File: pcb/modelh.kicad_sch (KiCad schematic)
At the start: 15 parts, among them J1 Battery Conn, J2 Conn_01x16, J3 Conn_01x12, J4 Conn_01x04, U1 nice_nano, U2 74HC595, U3 74HC595

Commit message: version 0.2
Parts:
- added D1, D10, D11, D12, D13, D14, D15, D16, D2, D3, D4, D5, D6, D7, D8, D9: D_Small, Library:DO-35 smaller, symbol Device:D_Small
- added J5: Conn_01x06, Connector_PinHeader_2.54mm:PinHeader_1x06_P2.54mm_Vertical, symbol Connector_Generic:Conn_01x06
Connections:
- net +3.3V: now also J5.2 (Pin_2); no longer JP5.2 (B)
- net CS: now also U1.8 (022); no longer U1.3 (008/RX)
- net GND: now also JP5.2 (B), J5.1 (Pin_1)
- net SCLK: now also U1.7 (020); no longer U1.2 (006/TX)
- net col0: now also D1.2 (A); no longer J2.1 (Pin_1)
- net col1: now also D2.2 (A); no longer J2.2 (Pin_2)
- net col10: now also D11.2 (A); no longer J2.11 (Pin_11)
- net col11: now also D12.2 (A); no longer J2.12 (Pin_12)
- net col12: now also D13.2 (A); no longer J2.13 (Pin_13)
- net col13: now also D14.2 (A); no longer J2.14 (Pin_14)
- net col14: now also D15.2 (A); no longer J2.15 (Pin_15)
- net col15: now also D16.2 (A); no longer J2.16 (Pin_16)
- net col2: now also D3.2 (A); no longer J2.3 (Pin_3)
- net col3: now also D4.2 (A); no longer J2.4 (Pin_4)
- net col4: now also D5.2 (A); no longer J2.5 (Pin_5)
- net col5: now also D6.2 (A); no longer J2.6 (Pin_6)
- net col6: now also D7.2 (A); no longer J2.7 (Pin_7)
- net col7: now also D8.2 (A); no longer J2.8 (Pin_8)
- net col8: now also D9.2 (A); no longer J2.9 (Pin_9)
- net col9: now also D10.2 (A); no longer J2.10 (Pin_10)
- net user4: now reaches U1.10 (100)
- net user4: now also J5.6 (Pin_6)
- net user3: now reaches U1.9 (024)
- net user3: now also J5.5 (Pin_5)
- new net: D1.1 (K), J2.1 (Pin_1)
- new net: D10.1 (K), J2.10 (Pin_10)
- new net: D11.1 (K), J2.11 (Pin_11)
- new net: D12.1 (K), J2.12 (Pin_12)
- new net: D13.1 (K), J2.13 (Pin_13)
- new net: D14.1 (K), J2.14 (Pin_14)
- new net: D15.1 (K), J2.15 (Pin_15)
- new net: D16.1 (K), J2.16 (Pin_16)
- new net: D2.1 (K), J2.2 (Pin_2)
- new net: D3.1 (K), J2.3 (Pin_3)
- new net: D4.1 (K), J2.4 (Pin_4)
- new net: D5.1 (K), J2.5 (Pin_5)
- new net: D6.1 (K), J2.6 (Pin_6)
- new net: D7.1 (K), J2.7 (Pin_7)
- new net: D8.1 (K), J2.8 (Pin_8)
- new net: D9.1 (K), J2.9 (Pin_9)
- new net user1: J5.3 (Pin_3), U1.2 (006/TX)
- new net user2: J5.4 (Pin_4), U1.3 (008/RX)
- no-connect marks 5 -> 1
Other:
- note added: "User"

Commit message: Rev 0.3
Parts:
- removed J2: Conn_01x16, Library:ModelH-triomate-cols16, symbol Connector_Generic:Conn_01x16
- added D17, D18, D19, D20: D_Small, Diode_SMD:D_SOD-123F, symbol Device:D_Small
- added J2: Conn_01x20, Library:ModelH-triomate-cols20, symbol Connector_Generic:Conn_01x20
- added U4: 74HC595, Package_DIP:DIP-16_W7.62mm_Socket_LongPads, symbol 74xx:74HC595
- D1, D10, D11, D12, D13, D14, D15, D16, D2, D3, D4, D5, D6, D7, D8, D9: footprint Library:DO-35 smaller -> Diode_SMD:D_SOD-123F
- U2, U3: footprint PCM_Package_DIP_AKL:DIP-16_W7.62mm_Socket_LongPads -> Package_DIP:DIP-16_W7.62mm_Socket_LongPads
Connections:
- net +3.3V: now also U4.10 (~{SRCLR}), U4.16 (VCC)
- net CS: now also U4.12 (RCLK)
- net GND: now also U4.13 (~{OE}), U4.8 (GND)
- net SCLK: now also U4.11 (SRCLK)
- net col0: now also U2.7 (QH); no longer U2.15 (QA)
- net col1: now also U2.6 (QG); no longer U2.1 (QB)
- net col10: now also U3.5 (QF); no longer U3.2 (QC)
- net col11: now also U3.4 (QE); no longer U3.3 (QD)
- net col12: now also U3.3 (QD); no longer U3.4 (QE)
- net col13: now also U3.2 (QC); no longer U3.5 (QF)
- net col14: now also U3.1 (QB); no longer U3.6 (QG)
- net col15: now also U3.15 (QA); no longer U3.7 (QH)
- net col2: now also U2.5 (QF); no longer U2.2 (QC)
- net col3: now also U2.4 (QE); no longer U2.3 (QD)
- net col4: now also U2.3 (QD); no longer U2.4 (QE)
- net col5: now also U2.2 (QC); no longer U2.5 (QF)
- net col6: now also U2.1 (QB); no longer U2.6 (QG)
- net col7: now also U2.15 (QA); no longer U2.7 (QH)
- net col8: now also U3.7 (QH); no longer U3.15 (QA)
- net col9: now also U3.6 (QG); no longer U3.1 (QB)
- net at D1.1 (K): now also J2.1 (Pin_1)
- net at D10.1 (K): now also J2.10 (Pin_10)
- net at D11.1 (K): now also J2.11 (Pin_11)
- net at D12.1 (K): now also J2.12 (Pin_12)
- net at D13.1 (K): now also J2.13 (Pin_13)
- net at D14.1 (K): now also J2.14 (Pin_14)
- net at D15.1 (K): now also J2.15 (Pin_15)
- net at D16.1 (K): now also J2.16 (Pin_16)
- net at D2.1 (K): now also J2.2 (Pin_2)
- net at D3.1 (K): now also J2.3 (Pin_3)
- net at D4.1 (K): now also J2.4 (Pin_4)
- net at D5.1 (K): now also J2.5 (Pin_5)
- net at D6.1 (K): now also J2.6 (Pin_6)
- net at D7.1 (K): now also J2.7 (Pin_7)
- net at D8.1 (K): now also J2.8 (Pin_8)
- net at D9.1 (K): now also J2.9 (Pin_9)
- net at U3.9 (QH'): now also U4.14 (SER)
- new net: D18.1 (K), J2.18 (Pin_18)
- new net: D19.1 (K), J2.19 (Pin_19)
- new net: D20.1 (K), J2.20 (Pin_20)
- new net: D17.1 (K), J2.17 (Pin_17)
- new net col16: D17.2 (A), U4.15 (QA)
- new net col17: D18.2 (A), U4.7 (QH)
- new net col18: D19.2 (A), U4.6 (QG)
- new net col19: D20.2 (A), U4.5 (QF)
- no-connect marks 1 -> 5
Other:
- note added: "Keyboard Matrix"
- moved on the sheet: J3, J4, J5, R7, R8, R9, U2, U3

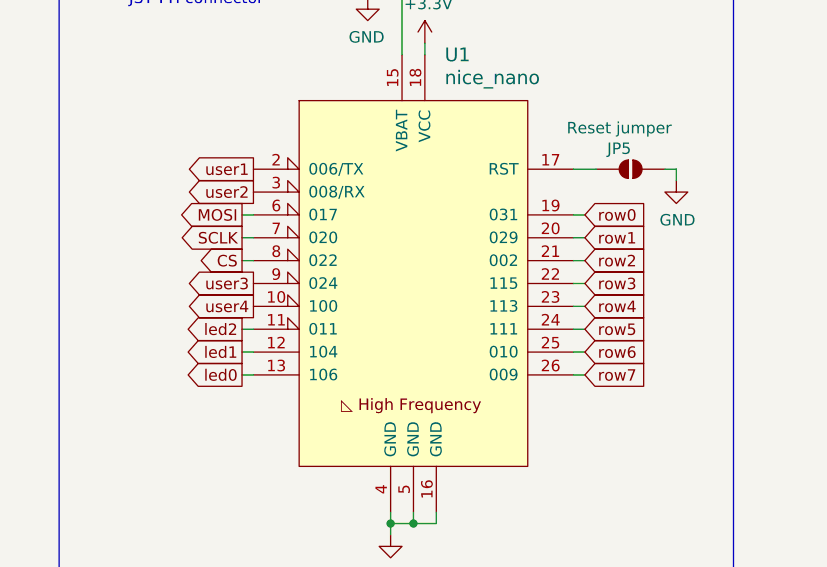
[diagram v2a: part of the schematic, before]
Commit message: Make it compatable with old pro micro
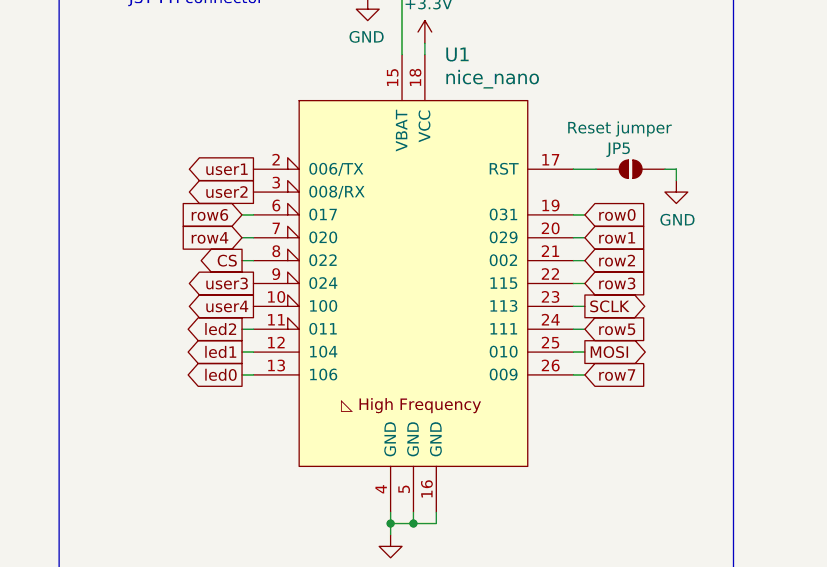
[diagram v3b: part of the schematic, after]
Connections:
- net MOSI: now also U1.25 (010); no longer U1.6 (017)
- net SCLK: now also U1.23 (113); no longer U1.7 (020)
- net row4: now also U1.7 (020); no longer U1.23 (113)
- net row6: now also U1.6 (017); no longer U1.25 (010)

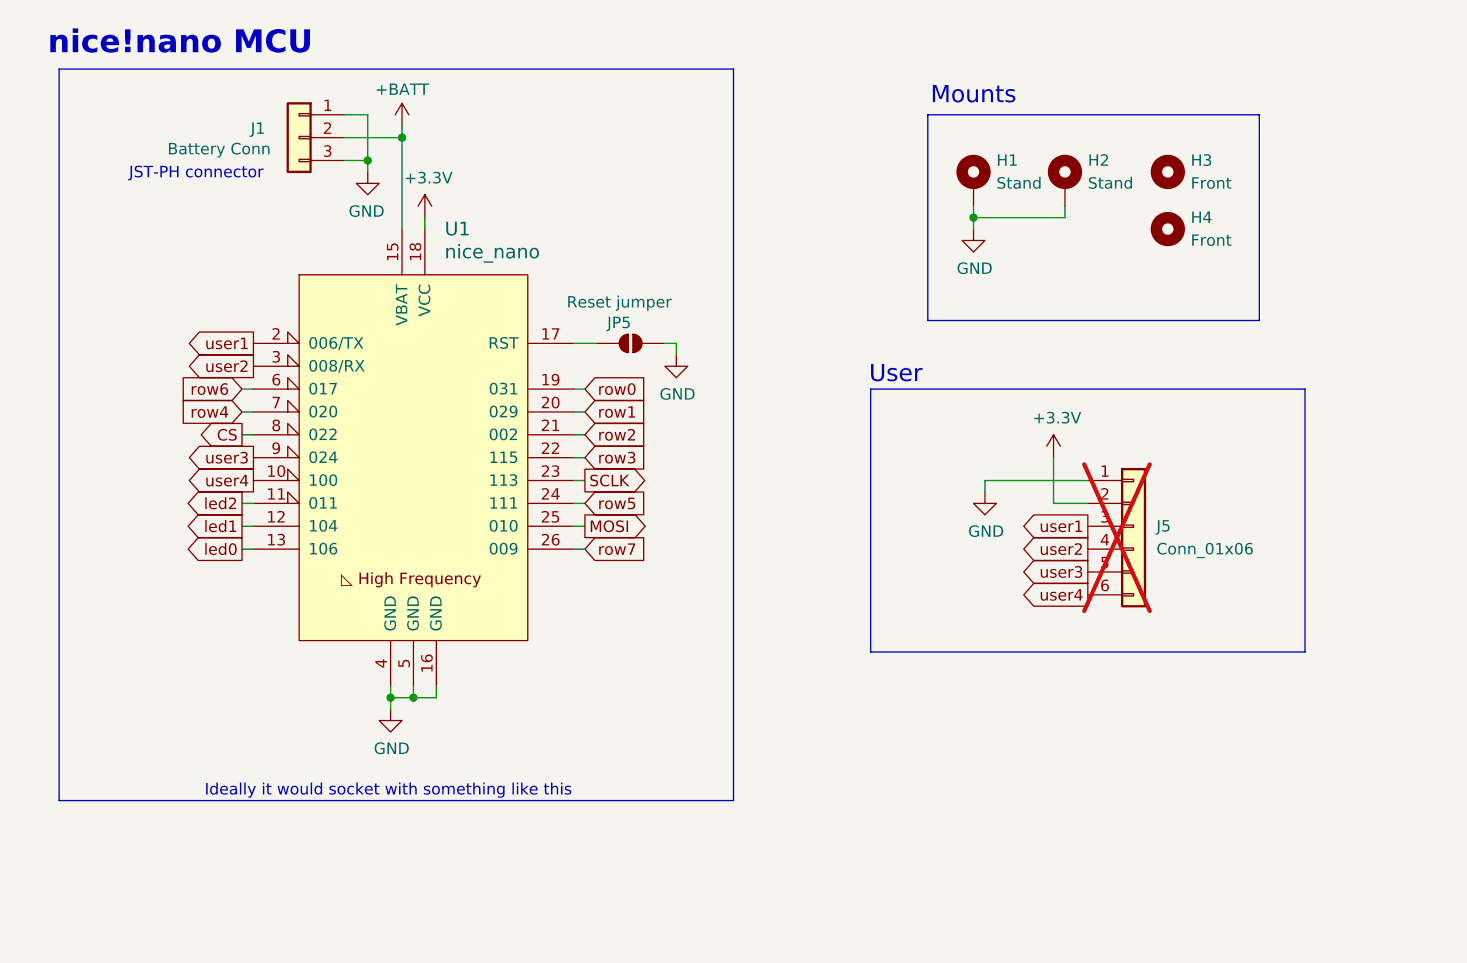
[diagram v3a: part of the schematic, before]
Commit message: v3.1; made it uncompatible because HF pins
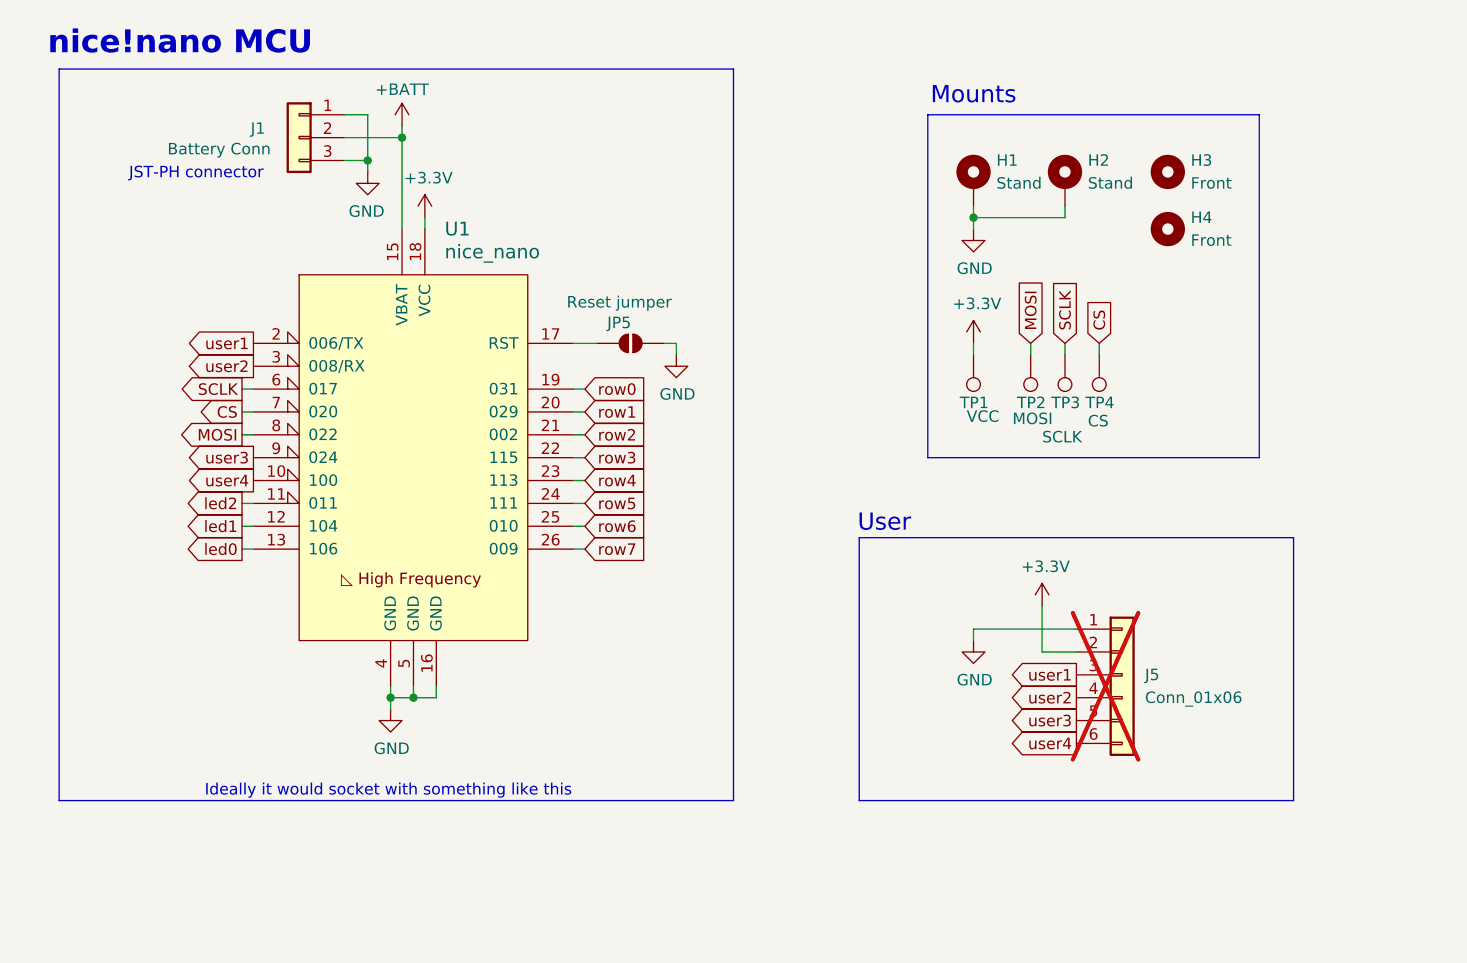
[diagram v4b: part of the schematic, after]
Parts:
- added TP1: VCC, TestPoint:TestPoint_Pad_D1.5mm, symbol Connector:TestPoint
- added TP2: MOSI, TestPoint:TestPoint_Pad_D1.0mm, symbol Connector:TestPoint
- added TP3: SCLK, TestPoint:TestPoint_Pad_D1.0mm, symbol Connector:TestPoint
- added TP4: CS, TestPoint:TestPoint_Pad_D1.0mm, symbol Connector:TestPoint
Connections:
- net +3.3V: now also TP1.1
- net CS: now also U1.7 (020), TP4.1; no longer U1.8 (022)
- net MOSI: now also U1.8 (022), TP2.1; no longer U1.25 (010)
- net SCLK: now also U1.6 (017), TP3.1; no longer U1.23 (113)
- net row4: now also U1.23 (113); no longer U1.7 (020)
- net row6: now also U1.25 (010); no longer U1.6 (017)
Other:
- moved on the sheet: J5

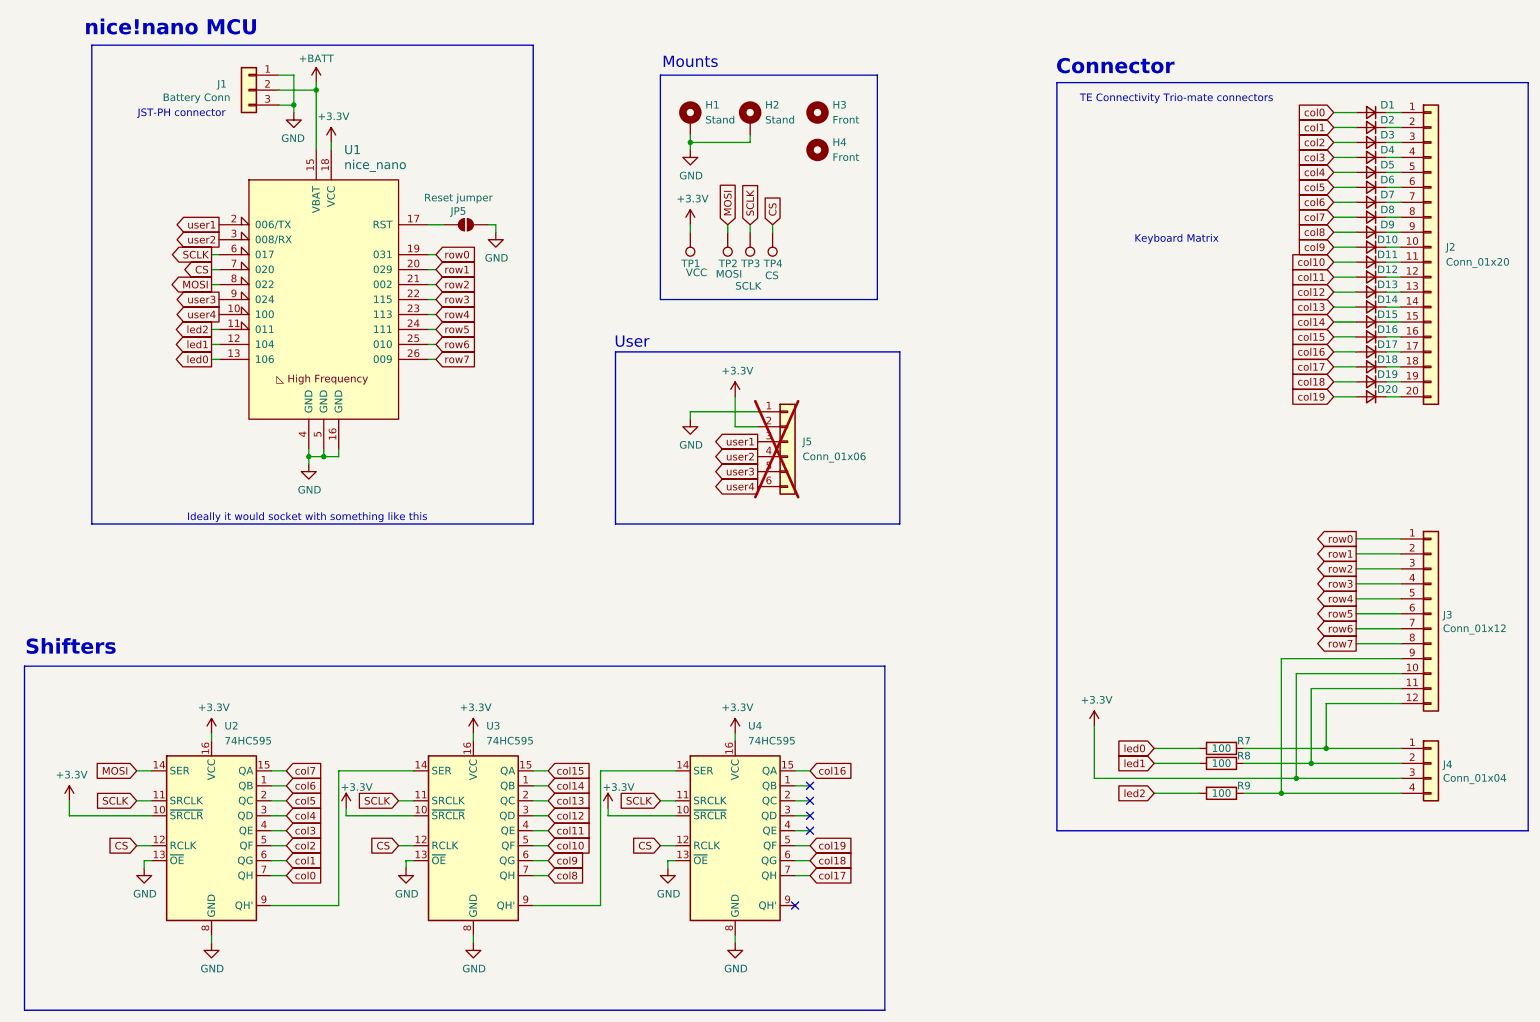
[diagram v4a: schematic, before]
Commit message: Added actual reset switch
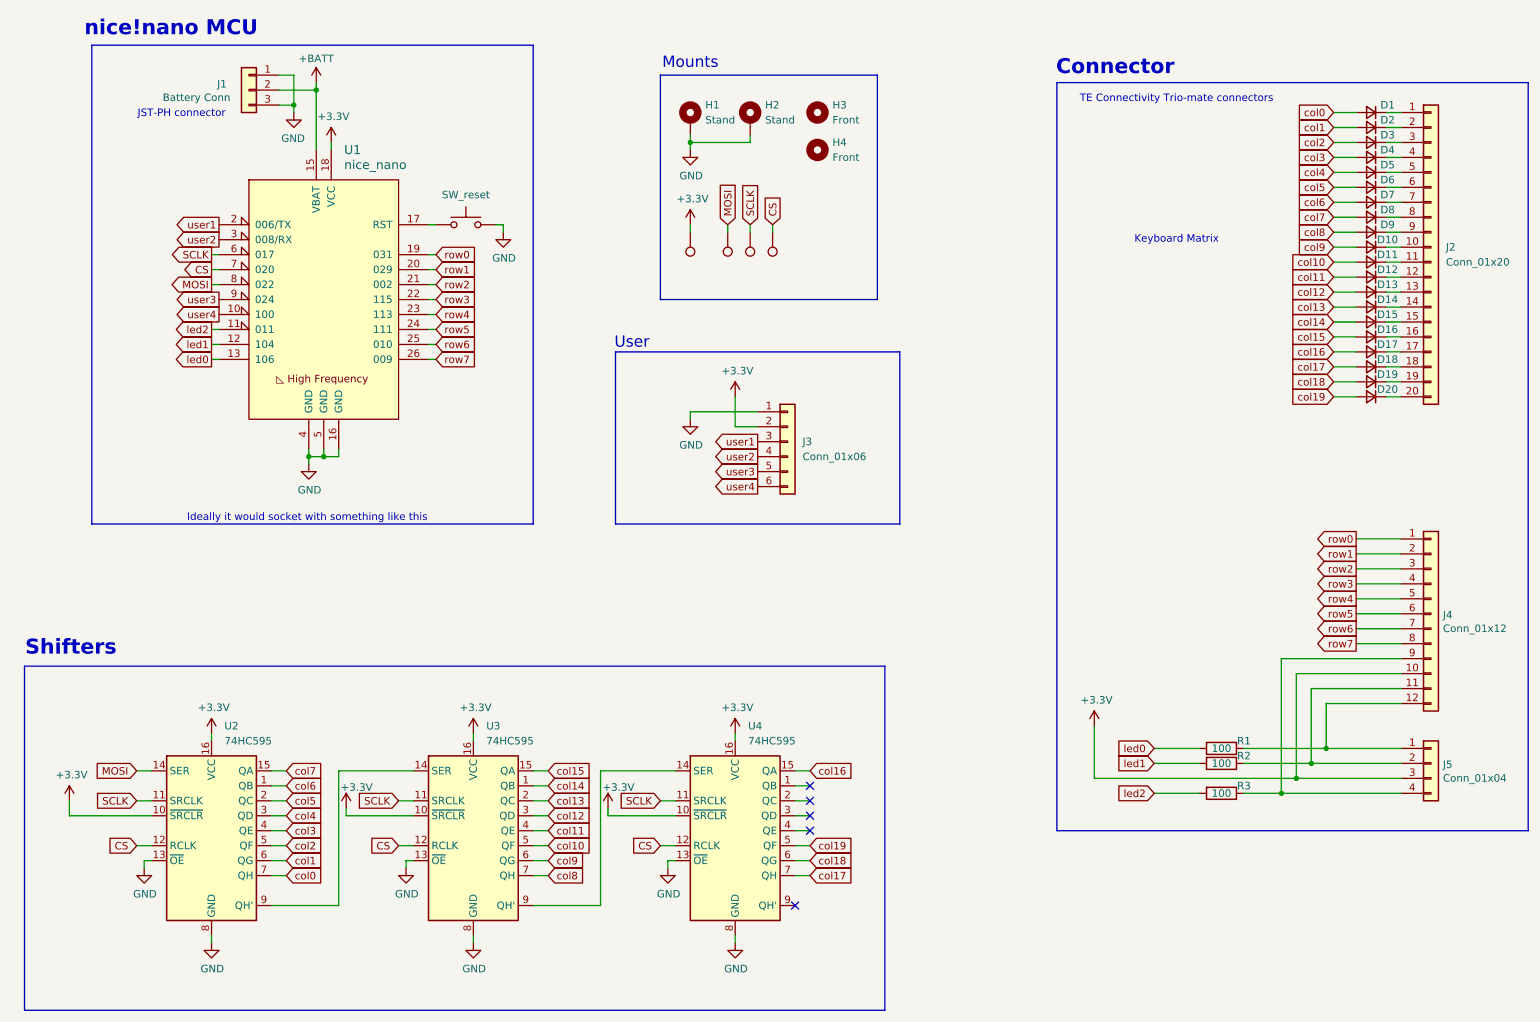
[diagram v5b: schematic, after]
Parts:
- removed JP5: Reset jumper, Jumper:SolderJumper-2_P1.3mm_Open_RoundedPad1.0x1.5mm, symbol Jumper:SolderJumper_2_Open
- added SW1: SW_reset, Button_Switch_THT:SW_PUSH_1P1T_6x3.5mm_H4.3_APEM_MJTP1243, symbol Switch:SW_Push
- J3: renamed from J5; now fitted
- TP1: footprint TestPoint:TestPoint_Pad_D1.5mm -> Library:TestPoint
- TP2, TP3, TP4: footprint TestPoint:TestPoint_Pad_D1.0mm -> Library:TestPoint
- renumbered J3 to J4, J4 to J5, R7 to R1, R8 to R2, R9 to R3
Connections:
- net GND: now also SW1.2
- net at U1.17 (RST): now also SW1.1
